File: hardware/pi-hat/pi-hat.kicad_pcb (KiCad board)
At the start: 4 copper layers, 65 x 56 mm, 75 parts, among them J1 PWR IN, J10 6-8, J11 PWM0, J12 PWM1, J13 KLPX-0848A-2-B, J14 KLPX-0848A-2-R, J2 A-F, J3 40HAT, J4 G-M, J5 N-Q, J6 PANEL_PWR, J7 PANEL_CTL, J8 2-5, J9 WP, Q1 DMG2305UX, Q2 DMMT5401, Q3 DMN6075S, Q4 NTR4171P, U1 CAT24C32, U10 L78L33_SOT89, U11 L78L33_SOT89, U12 PCM5122PW, U2 CM1293A, U3 CM1293A, U4 CM1293A, U5 CM1293A, U6 CM1293A, U7 CM1293A, U8 MCP23S17_SO, U9 MCP23S17_SO

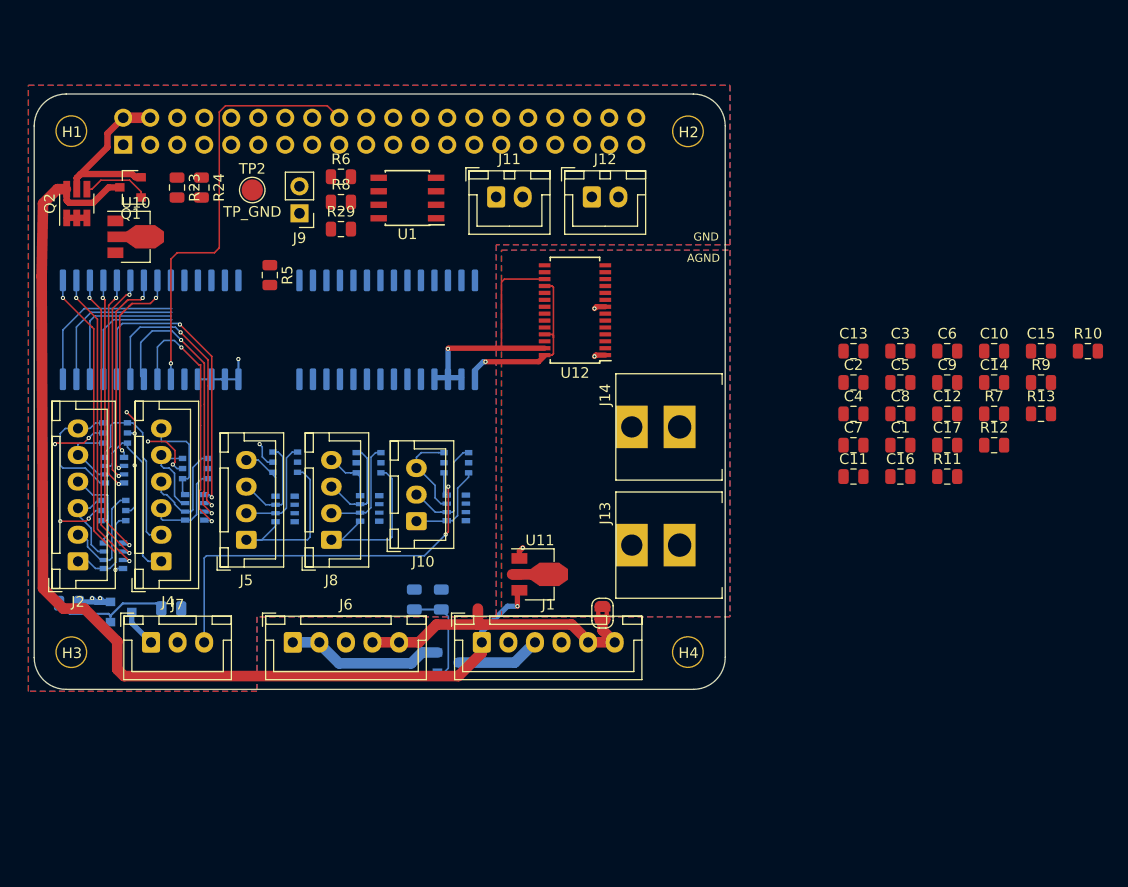
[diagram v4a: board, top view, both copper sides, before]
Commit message: fully routed
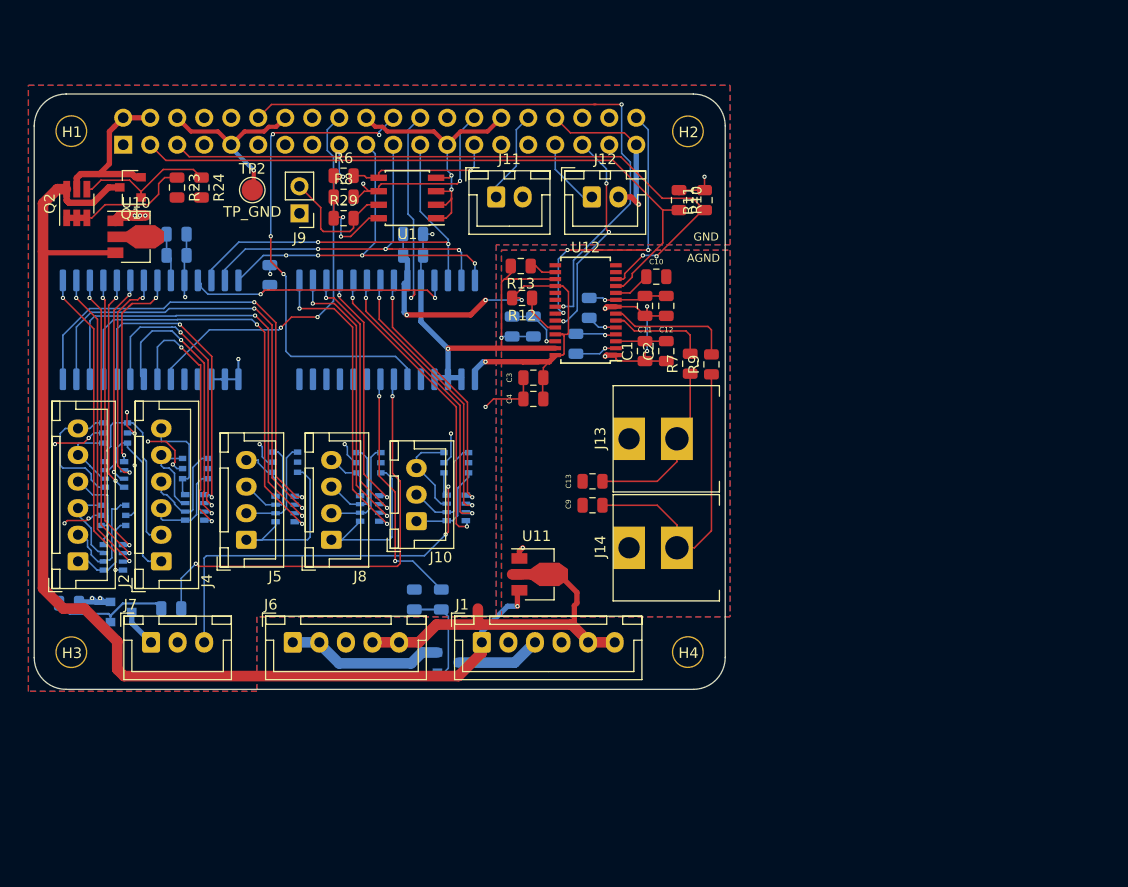
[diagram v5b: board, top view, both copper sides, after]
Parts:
- C14, C15, C16, C17, C5, C6, C7, C8, R5: moved to B.Cu
- JP1: footprint Jumper:SolderJumper-2_P1.3mm_Bridged2Bar_RoundedPad1.0x1.5mm -> NetTie:NetTie-2_SMD_Pad0.5mm
- moved C15 82.1 mm to (91.9, 74.0)
- moved C14 77.8 mm to (91.9, 76.0)
- moved C17 54.0 mm to (114.2, 74.0)
- moved R13 50.9 mm to (124.3, 77.0), turned to 180 degrees
- moved C16 50.3 mm to (114.2, 76.0)
- moved R12 46.5 mm to (124.4, 80.0), turned to 180 degrees
- moved R10 41.0 mm to (139.2, 70.8), turned to 270 degrees
- moved C6 41.0 mm to (123.5, 82.7), turned to 270 degrees
- moved C9 35.3 mm to (131.1, 99.5)
- moved C5 34.9 mm to (125.5, 82.7), turned to 270 degrees
- moved C3 34.6 mm to (125.5, 87.5), turned to 180 degrees
- moved R11 34.6 mm to (141.6, 70.8), turned to 270 degrees
- moved C10 32.5 mm to (137.1, 78.0)
- moved R9 31.0 mm to (142.2, 86.2), turned to 90 degrees
- moved C8 30.9 mm to (130.8, 80.9), turned to 270 degrees
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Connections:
- U8 pad 18: GND -> (no net)
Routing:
- net GND: track 81.5 -> 178.8 mm, vias 11 -> 22
- net /I2C_SCL: track 0.00 -> 63.5 mm, vias 0 -> 2
- net /I2C_SDA: track 0.00 -> 61.8 mm
- net /PCM_CLK: track 0.00 -> 58.2 mm, vias 0 -> 2
- net /IO_INT_B: track 0.00 -> 46.5 mm, vias 0 -> 4
- net /SPI_CS: track 0.00 -> 45.0 mm, vias 0 -> 3
- net /P3V3: track 27.6 -> 72.4 mm, vias 4 -> 11
- net /SOLENOID_SW: track 0.00 -> 41.9 mm, vias 0 -> 2
- net /SPI_CLK: track 0.00 -> 38.3 mm, vias 0 -> 2
- net /SPI_MOSI: track 0.00 -> 37.5 mm, vias 0 -> 3
- net /SPI_MISO: track 0.00 -> 36.4 mm, vias 0 -> 4
- net /N: track 11.5 -> 41.0 mm, vias 0 -> 2
- net /P: track 14.5 -> 43.9 mm, vias 0 -> 2
- net /O: track 13.3 -> 42.7 mm, vias 0 -> 2
- net /2: track 0.00 -> 29.1 mm, vias 0 -> 2
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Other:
- copper layers 4 -> 2
- board text added: "P3V3"
- board text added: "P3V3A"

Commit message: fiddle with groundplanes and gnd routing
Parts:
- C5, C6: moved to F.Cu
- moved C4 2.71 mm to (125.0, 86.8), turned to 90 degrees
- moved C3 2.49 mm to (123.1, 86.8), turned to 90 degrees
- moved R13 0.65 mm to (123.7, 77.3)
- moved R12 0.63 mm to (123.8, 79.8)
- moved C1 0.60 mm to (135.4, 85.0)
- moved C2 0.60 mm to (137.4, 85.0)
- moved C5 0.50 mm to (125.0, 82.7)
- moved C6 0.40 mm to (123.1, 82.7)
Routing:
- net GND: track 178.8 -> 138.8 mm, vias 22 -> 16
- net /P3V3: track 72.4 -> 53.7 mm, vias 11 -> 9
- net /R_CHAN: track 28.5 -> 25.4 mm
- net /SOLENOID_SW: track 41.9 -> 42.6 mm, vias 2 -> 4
- net /P3V3A: track 19.7 -> 19.2 mm, vias 5 -> 4
- net /LDOO: track 5.66 -> 5.87 mm, vias 1 -> 0

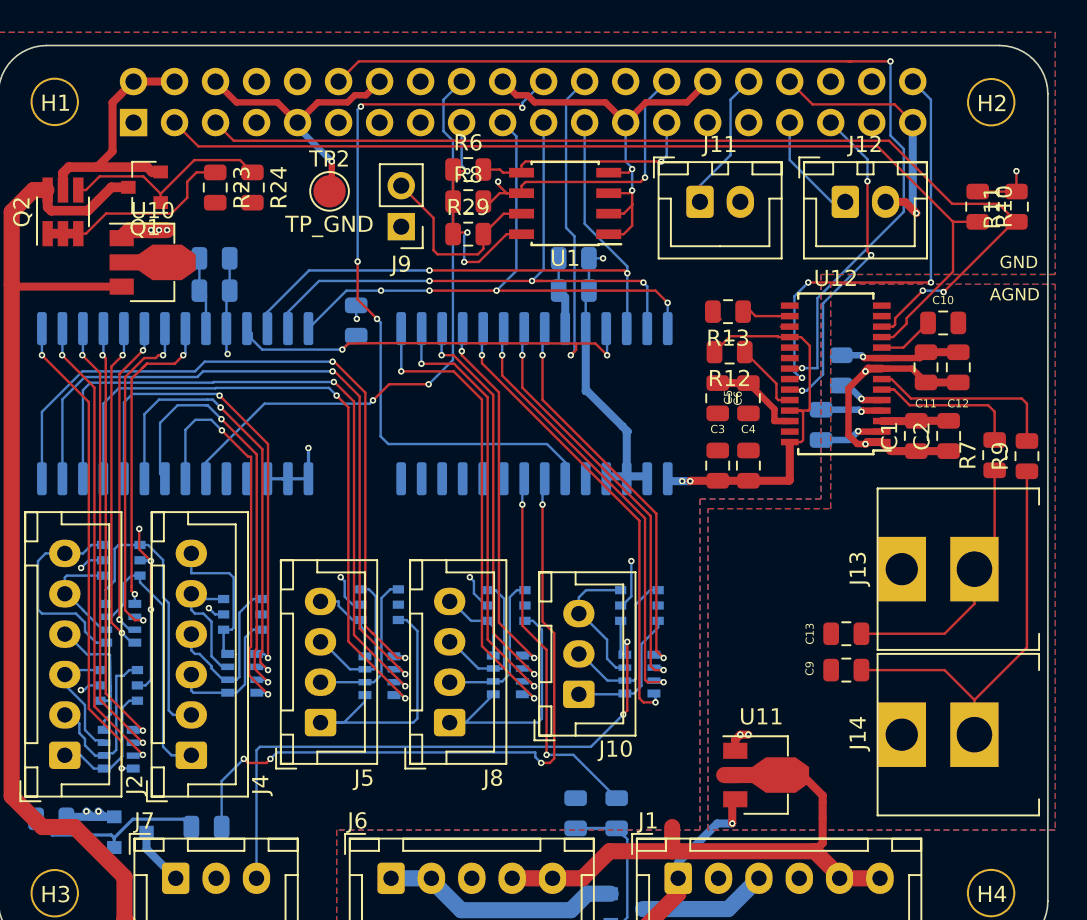
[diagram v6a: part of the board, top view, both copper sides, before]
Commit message: add icons and voltage testpoints
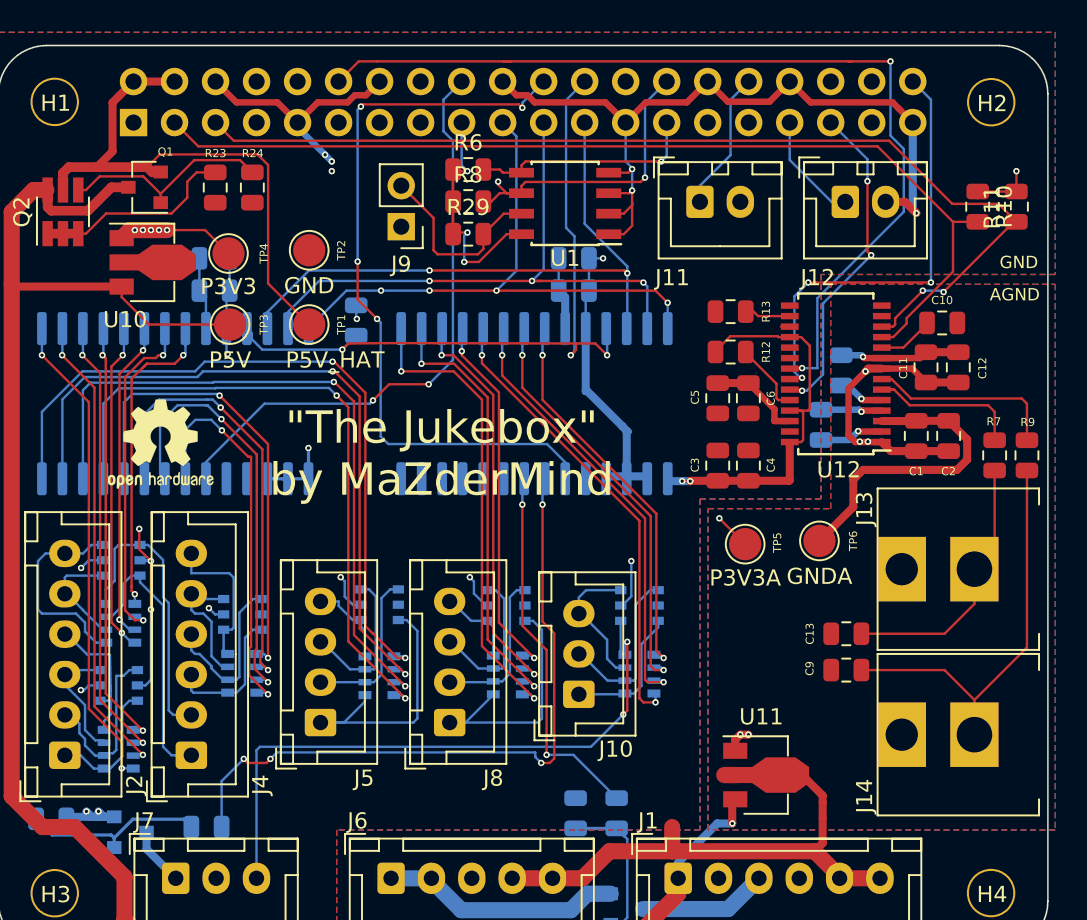
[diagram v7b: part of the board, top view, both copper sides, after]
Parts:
- added OSHW1: Logo_Open_Hardware_Large, Symbol:OSHW-Logo2_7.3x6mm_SilkScreen, F.Cu at (88.6, 85.5)
- added TP1: P5V_HAT, TestPoint:TestPoint_Pad_D2.0mm, F.Cu at (97.8, 78.1)
- added TP3: P5V, TestPoint:TestPoint_Pad_D2.0mm, F.Cu at (92.9, 78.1)
- added TP4: P3V3, TestPoint:TestPoint_Pad_D2.0mm, F.Cu at (92.8, 73.7)
- added TP5: P3V3A, TestPoint:TestPoint_Pad_D2.0mm, F.Cu at (124.8, 91.7)
- added TP6: GNDA, TestPoint:TestPoint_Pad_D2.0mm, F.Cu at (129.4, 91.5)
- TP2: value TP_GND -> GND
- moved TP2 3.86 mm to (97.8, 73.5)
- moved R13 0.16 mm to (123.9, 77.3)
- moved C10 0.06 mm to (137.0, 78.0)
- moved R12 0.06 mm to (123.9, 79.8)
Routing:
- net /P5V_HAT: track 16.2 -> 35.2 mm
- net GNDA: track 15.1 -> 30.3 mm
- net /P5V: track 107.5 -> 115.6 mm
- net /P3V3: track 53.7 -> 59.1 mm, vias 9 -> 11
- net GND: track 138.8 -> 143.0 mm, vias 16 -> 18
- net /P3V3A: track 19.2 -> 21.3 mm, vias 4 -> 6
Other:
- board text added: ""The Jukebox" by MaZderMind"

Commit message: add indicator led
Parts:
- added D1: LED GN, LED_SMD:LED_0603_1608Metric, F.Cu at (104.3, 90.0)
- added R14: 100R, Resistor_SMD:R_0805_2012Metric, F.Cu at (107.2, 90.3)
- moved OSHW1 0.50 mm to (88.6, 85.0)
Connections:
- U9 pad 28: (no net) -> Net-(D1-Pad2)
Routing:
- net Net-(D1-Pad2): track 0.00 -> 3.11 mm, vias 0 -> 1
- net Net-(D1-Pad1): track 0.00 -> 2.64 mm
- net GND: track 143.0 -> 141.1 mm, vias 18 -> 19
- net /P5V: track 115.6 -> 116.6 mm, vias 1 -> 3
- net /P3V3A: vias 6 -> 8
- net /P3V3: vias 11 -> 9
